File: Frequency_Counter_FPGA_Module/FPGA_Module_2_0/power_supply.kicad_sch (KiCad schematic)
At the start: 51 parts, among them U16 LMR33630ADDAR, U17 B0505S-1W, U18 LMR33630ADDAR

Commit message: feat(boot): LED selftest blikaci kod + RTC LSE medium-low drive; UI 4.3" audit; FPGA HW revize
STM32H757 firmware:
- bootled.c/h: boot-time HW selftest diagnostika na LED_1 (PG3). Kazdy
  sledovany periferni init (FMC/SPI2/I2C4/DSIHOST/LTDC/USART1/RTC/ADC3/
  QUADSPI/I2C1) + display bring-up (panel probe/power-on/DSI start/
  TC358762) si zaznamena poradove cislo; pri zaseknuti v Error_Handler()
  LED bez displeje zabliká N-krat podle poradi. Regen-safe (jen chranene
  USER CODE hooky), bez zpozdeni v happy-path.
- RTC LSE Drive Capability LOW -> MEDIUM LOW (H757_LED.ioc): kompenzuje
  desky s predimenzovanymi zatezovymi kondenzatory krystalu (22pF misto
  18pF), ktere LSE nerozjizdely.
- UI audit pro realny 4,3" 800x480 panel (8,54 px/mm): hit-slop pilulek,
  fonty, HDR_PILL_LIMIT fit-check, Menu 3x4 mrizka s placeholdery, oprava
  ghost bugu AUTO CET/CEST tlacitka, sign-loss bug ve fmt_fixed/fmt_minmax.
  main-old layout zamrazen jako default (A/B srovnani, viz STATUS.md #14).

FPGA carrier v2.0 (KiCad): prubezne review checklisty a schema/PCB revize.

Co-Authored-By: OK2JNJ <ok2jnj@local>
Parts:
- renumbered C79 to C100, C93 to C101, C80 to C102, C81 to C103, C94 to C104, C82 to C105, C95 to C106, C83 to C107, C96 to C108, C84 to C109, C85 to C110, C97 to C111, C87 to C112, C98 to C113, C86 to C114, C88 to C115, C89 to C116, C99 to C117, C90 to C118, C77 to C96, C91 to C97, C78 to C98, C92 to C99, D5 to D4, D4 to D5, F3 to F2, F2 to F3, L3 to L1, L6 to L2, L4 to L3, L5 to L4, L7 to L5, R79 to R100, R76 to R101, R80 to R102, R77 to R103, R73 to R95, R48 to R96, R74 to R97, R75 to R98, R78 to R99, U16 to U23, U18 to U24, U17 to U25

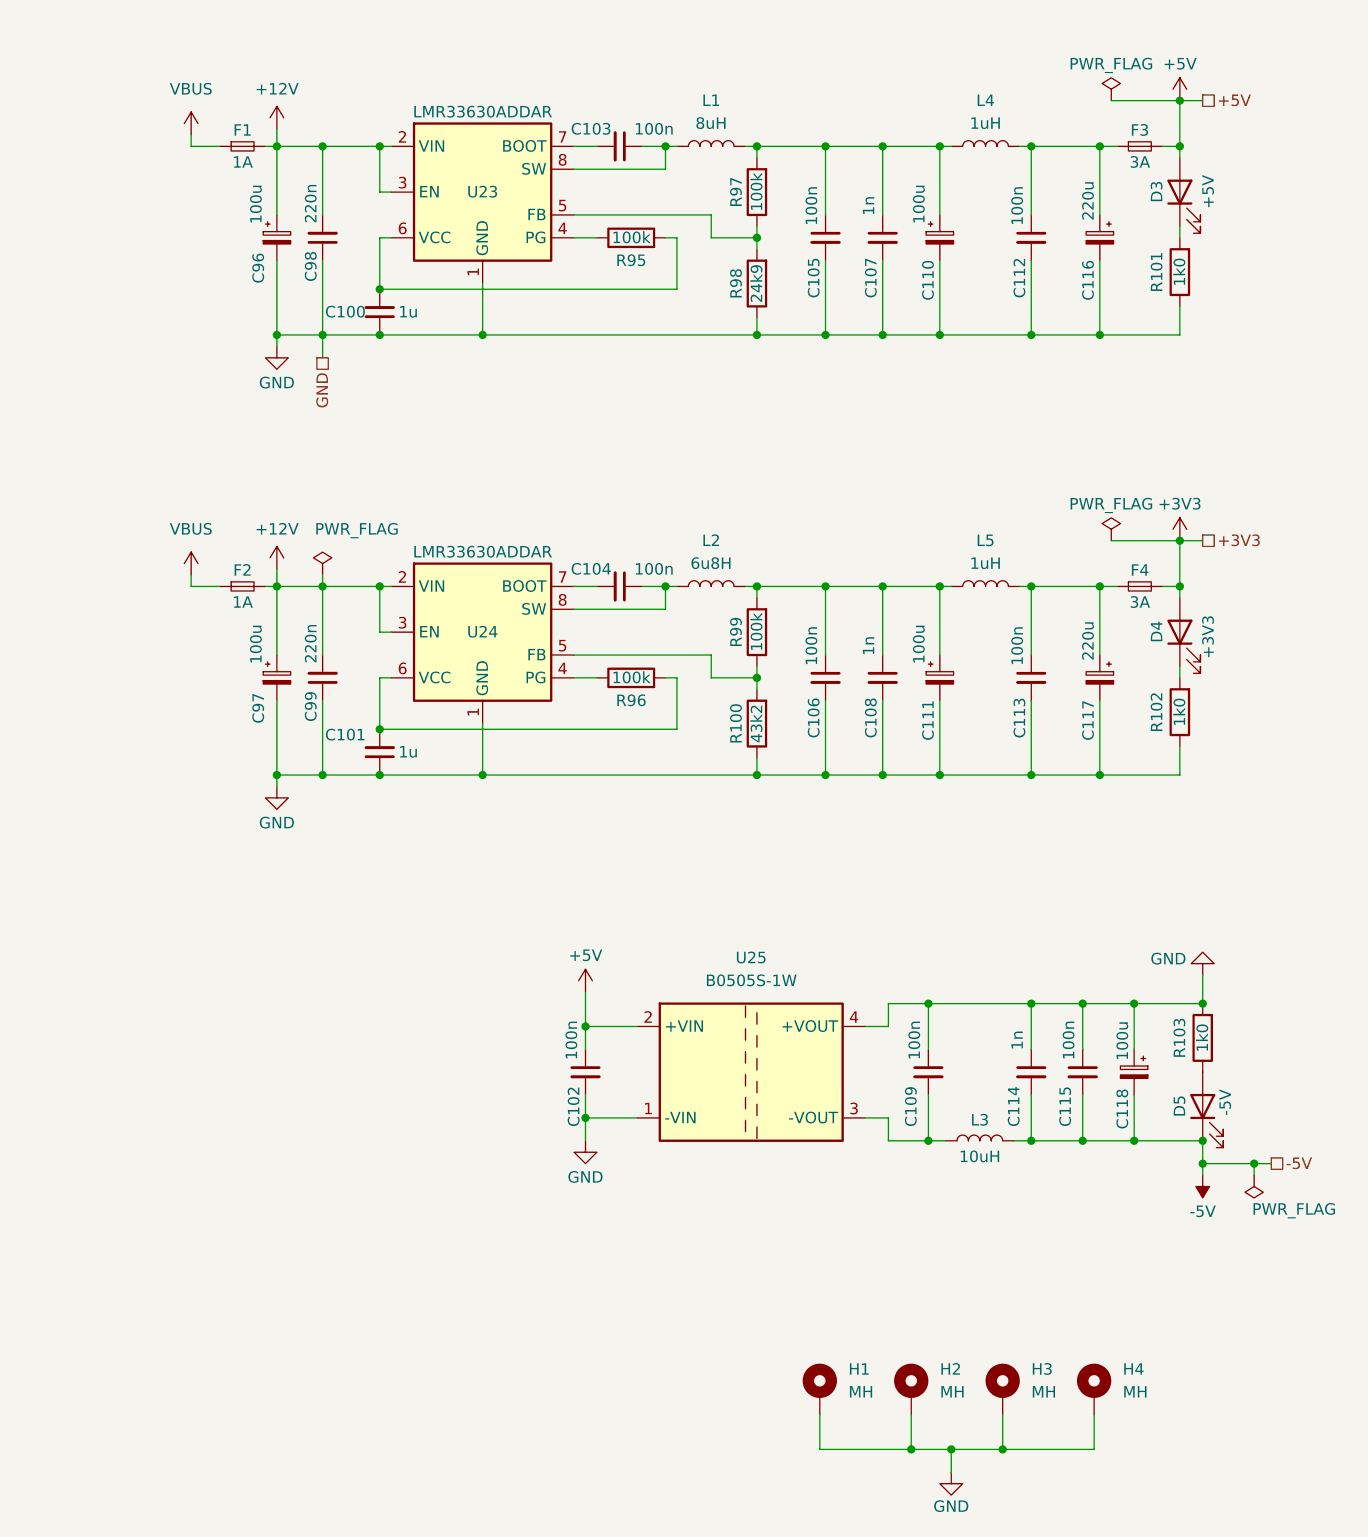
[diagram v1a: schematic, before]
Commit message: feat(hw): FPGA carrier v2.0 — aktualizace schematu + PCB + checklist
KiCad FPGA_Module_2_0 (FPGA_Core/GPSDO/I2C_devices/power_supply schemata,
PCB layout, project), BOARD_V20_CHECKLIST.md. Odstranen zastaraly
FPGA_module_schematic.pdf (nahrazen exportem FPGA_module.pdf).

Co-Authored-By: OK2JNJ <ok2jnj@users.noreply.github.com>
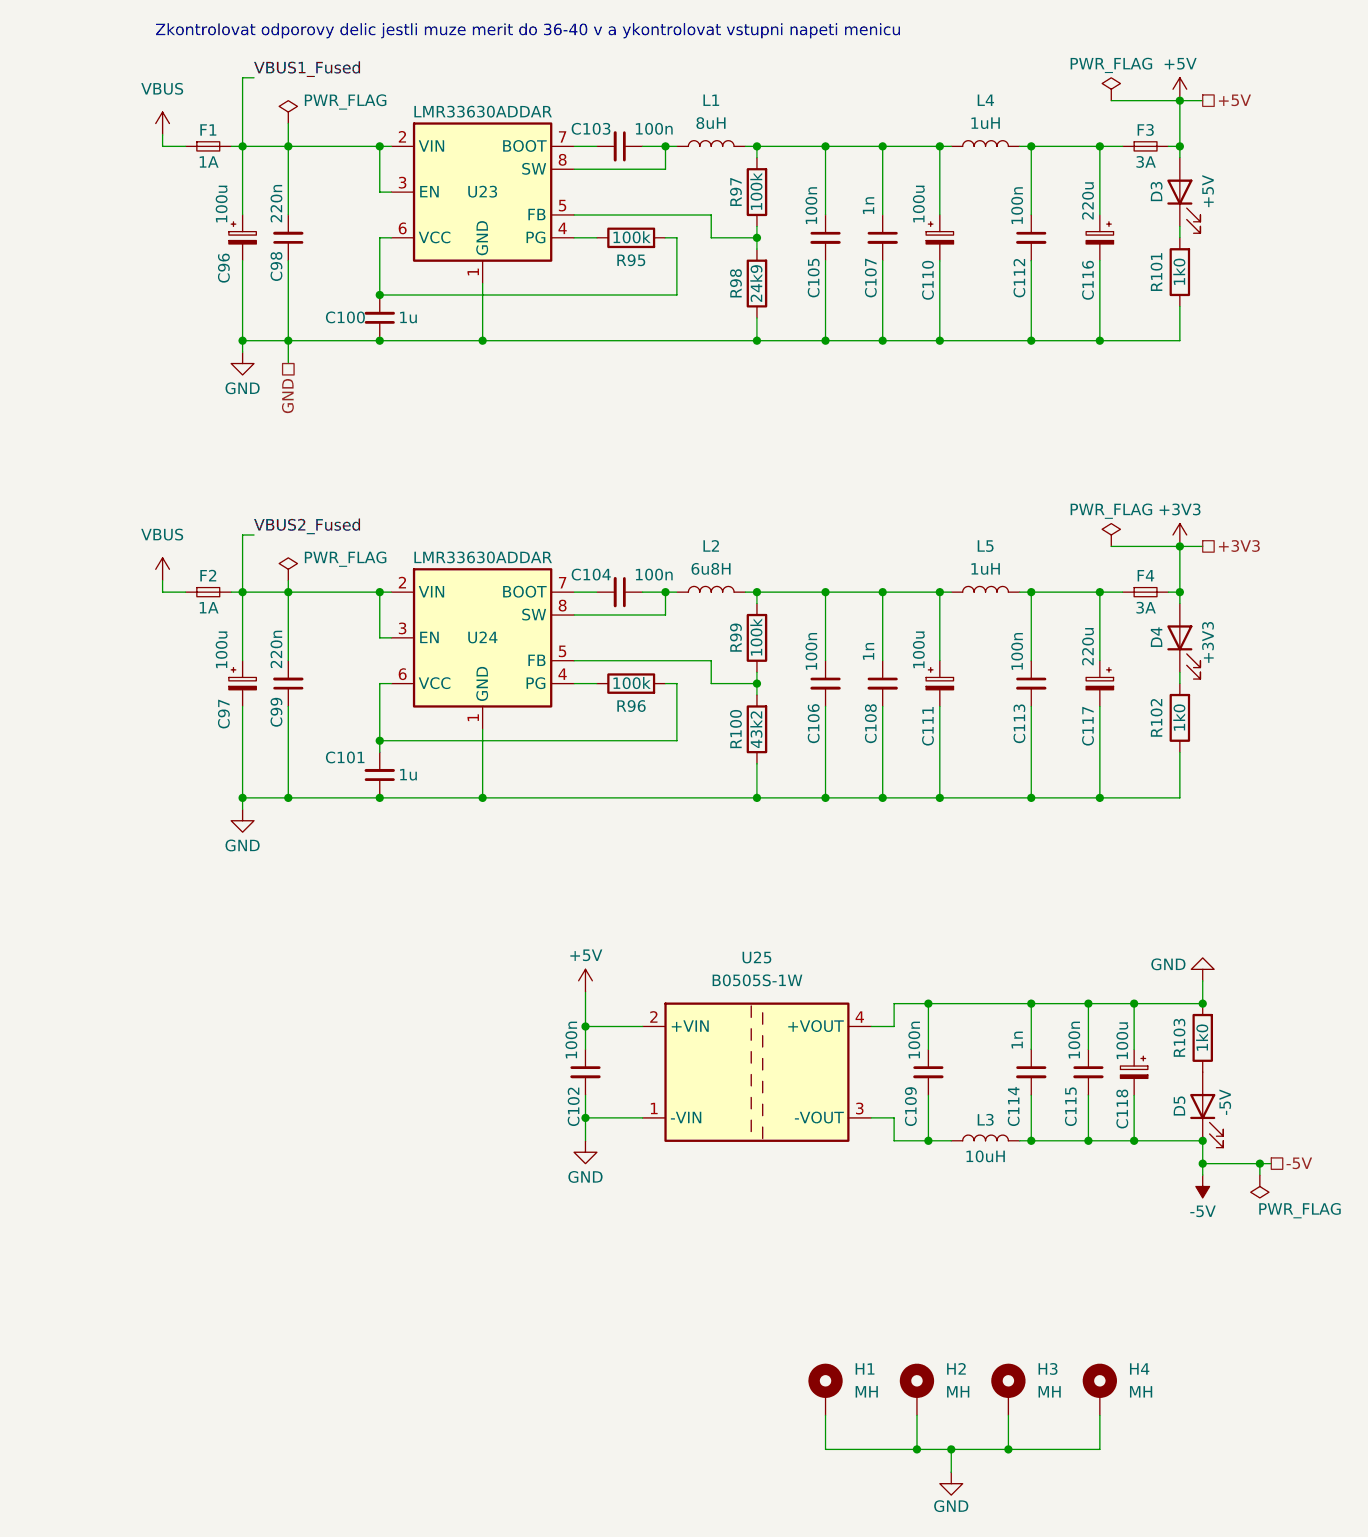
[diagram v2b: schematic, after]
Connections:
- net +12V renamed VBUS1_Fused
- net VBUS1_Fused: no longer C97.1, C99.2, F2.2, U24.2 (VIN), U24.3 (EN)
- new net VBUS2_Fused: C97.1, C99.2, F2.2, U24.2 (VIN), U24.3 (EN)
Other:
- note added: "Zkontrolovat odporovy delic jestli muze merit do 36-40 v a ykontrolovat vstupni napeti menicu"
- moved on the sheet: C100, C101, C104, C106, C108, C111, C113, C115, C117, C96, C97, C98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
